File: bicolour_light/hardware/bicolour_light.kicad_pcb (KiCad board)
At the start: 2 copper layers, 12.6 x 11 mm, 6 parts, among them J1 PIN_A, J2 PIN_B

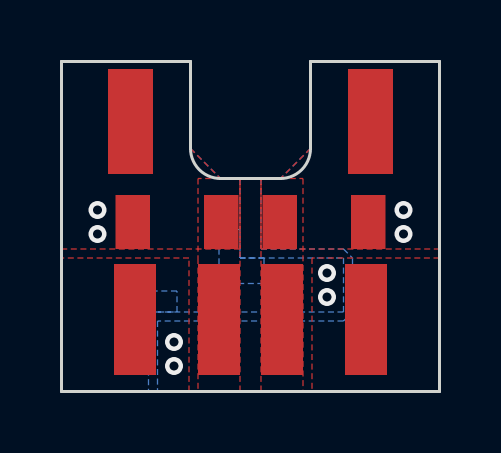
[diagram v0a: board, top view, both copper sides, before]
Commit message: Added polar light (single yellow LED)
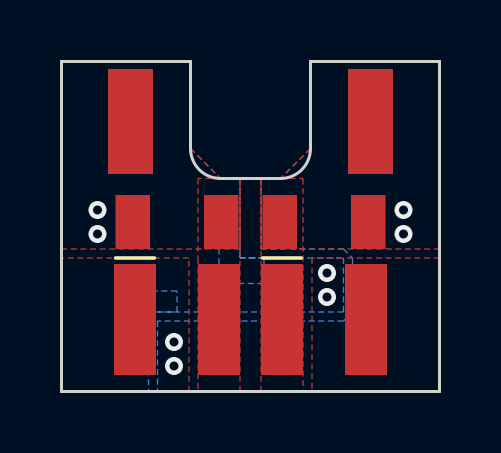
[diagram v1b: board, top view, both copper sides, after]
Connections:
- D1 pad 1: Net-(D1-KA) -> /PIN_B
- D1 pad 2: /PIN_B -> Net-(D1-AK)
- D2 pad 1: /PIN_A -> Net-(D2-KA)
- D2 pad 2: Net-(D2-AK) -> /PIN_A
- R1 pad 2: Net-(D1-KA) -> Net-(D1-AK)
- R2 pad 1: Net-(D2-AK) -> Net-(D2-KA)
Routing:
- added copper zone on F.Cu, net Net-(D1-AK)
- added copper zone on F.Cu, net Net-(D2-KA)
- removed copper zone on F.Cu, net Net-(D1-KA)
- removed copper zone on F.Cu, net Net-(D2-AK)
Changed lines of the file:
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@@
   (net 1 "/PIN_B")
   (net 2 "/PIN_A")
-  (net 3 "Net-(D1-KA)")
-  (net 4 "Net-(D2-AK)")
+  (net 3 "Net-(D1-AK)")
+  (net 4 "Net-(D2-KA)")
   (footprint "Slonket_Footprints:D_LED_4040" (layer "F.Cu")
     (at 126.65 94.55 180)
     (property "LCSC" "C7545694")
-    (property "Sheetfile" "LED_light.kicad_sch")
+    (property "Sheetfile" "bicolour_light.kicad_sch")
     (property "Sheetname" "")
     (property "ki_description" "Dual LED, bidirectional")
@@
         (effects (font (size 0.75 0.75) (thickness 0.1)))
     )
+    (fp_line (start 2.05 2.4) (end 0.75 2.4)
+      (stroke (width 0.12) (type default)) (layer "F.SilkS"))
     (fp_rect (start -2.35 2.45) (end 2.35 -2.05)
       (stroke (width 0.05) (type default)) (fill none) (layer "F.CrtYd"))
-    (fp_line (start -2 -1.3) (end -1.5 -1.8)
-      (stroke (width 0.1) (type default)) (layer "F.Fab"))
-    (fp_line (start -2 1.8) (end -2 -1.3)
-      (stroke (width 0.1) (type default)) (layer "F.Fab"))
-    (fp_line (start -1.5 -1.8) (end 2 -1.8)
-      (stroke (width 0.1) (type default)) (layer "F.Fab"))
-    (fp_line (start 2 -1.8) (end 2 1.8)
-      (stroke (width 0.1) (type default)) (layer "F.Fab"))
-    (fp_line (start 2 1.8) (end -2 1.8)
-      (stroke (width 0.1) (type default)) (layer "F.Fab"))
-    (pad "1" smd rect (at -1.4 0.35 180) (size 1.4 3.7) (layers "F.Cu" "F.Paste" "F.Mask")
-      (net 3 "Net-(D1-KA)") (pinfunction "KA") (pintype "input") (thermal_bridge_angle 45))
-    (pad "2" smd rect (at 1.4 0.35 180) (size 1.4 3.7) (layers "F.Cu" "F.Paste" "F.Mask")
-      (net 1 "/PIN_B") (pinfunction "AK") (pintype "input") (thermal_bridge_angle 45))
+    (fp_line (start -2 -1.8) (end 2 -1.8)
+      (stroke (width 0.1) (type default)) (layer "F.Fab"))
+    (fp_line (start -2 1.8) (end -2 -1.8)
+      (stroke (width 0.1) (type default)) (layer "F.Fab"))
+    (fp_line (start 1.5 1.8) (end -2 1.8)
+      (stroke (width 0.1) (type default)) (layer "F.Fab"))
+    (fp_line (start 2 -1.8) (end 2 1.3)
+      (stroke (width 0.1) (type default)) (layer "F.Fab"))
+    (fp_line (start 2 1.3) (end 1.5 1.8)
+      (stroke (width 0.1) (type default)) (layer "F.Fab"))
+    (pad "1" smd rect (at 1.4 0.35 180) (size 1.4 3.7) (layers "F.Cu" "F.Paste" "F.Mask")
+      (net 1 "/PIN_B") (pinfunction "KA") (pintype "input") (thermal_bridge_angle 45))
+    (pad "2" smd rect (at -1.4 0.35 180) (size 1.4 3.7) (layers "F.Cu" "F.Paste" "F.Mask")
+      (net 3 "Net-(D1-AK)") (pinfunction "AK") (pintype "input") (thermal_bridge_angle 45))
     (model "../3D_models/LED4040.step"
       (offset (xyz 0 1.8 0))
@@
     (at 126.65 90.95)
     (property "LCSC" "C25386")
-    (property "Sheetfile" "LED_light.kicad_sch")
+    (property "Sheetfile" "bicolour_light.kicad_sch")
     (property "Sheetname" "")
     (property "ki_description" "Resistor")
@@
       (net 2 "/PIN_A") (pintype "passive"))
     (pad "2" smd rect (at 1.475 0) (size 1.15 1.8) (layers "F.Cu" "F.Paste" "F.Mask")
-      (net 3 "Net-(D1-KA)") (pintype "passive"))
+      (net 3 "Net-(D1-AK)") (pintype "passive"))
     (model "${KICAD6_3DMODEL_DIR}/Resistor_SMD.3dshapes/R_1206_3216Metric.wrl"
       (offset (xyz 0 0 0))
@@
     (at 131.55 90.95)
     (property "LCSC" "C25386")
-    (property "Sheetfile" "LED_light.kicad_sch")
+    (property "Sheetfile" "bicolour_light.kicad_sch")
     (property "Sheetname" "")
     (property "ki_description" "Resistor")
@@
       (stroke (width 0.1) (type solid)) (layer "F.Fab"))
     (pad "1" smd rect (at -1.475 0) (size 1.15 1.8) (layers "F.Cu" "F.Paste" "F.Mask")
-      (net 4 "Net-(D2-AK)") (pintype "passive"))
+      (net 4 "Net-(D2-KA)") (pintype "passive"))
     (pad "2" smd rect (at 1.475 0) (size 1.15 1.8) (layers "F.Cu" "F.Paste" "F.Mask")
       (net 1 "/PIN_B") (pintype "passive"))
@@
   (footprint "Slonket_Footprints:J_Pad_1_Lego" (layer "F.Cu")
     (at 125.1 87.6 180)
-    (property "Sheetfile" "LED_light.kicad_sch")
+    (property "Sheetfile" "bicolour_light.kicad_sch")
     (property "Sheetname" "")
     (property "ki_description" "Generic connector, single row, 01x01, script generated (kicad-library-utils/schlib/autogen/connector/)")
@@
     (at 131.55 94.55 180)
     (property "LCSC" "C7545694")
-    (property "Sheetfile" "LED_light.kicad_sch")
+    (property "Sheetfile" "bicolour_light.kicad_sch")
     (property "Sheetname" "")
     (property "ki_description" "Dual LED, bidirectional")
@@
         (effects (font (size 0.75 0.75) (thickness 0.1)))
     )
+    (fp_line (start 2.05 2.4) (end 0.75 2.4)
+      (stroke (width 0.12) (type default)) (layer "F.SilkS"))
     (fp_rect (start -2.35 2.45) (end 2.35 -2.05)
       (stroke (width 0.05) (type default)) (fill none) (layer "F.CrtYd"))
-    (fp_line (start -2 -1.3) (end -1.5 -1.8)
-      (stroke (width 0.1) (type default)) (layer "F.Fab"))
-    (fp_line (start -2 1.8) (end -2 -1.3)
-      (stroke (width 0.1) (type default)) (layer "F.Fab"))
-    (fp_line (start -1.5 -1.8) (end 2 -1.8)
-      (stroke (width 0.1) (type default)) (layer "F.Fab"))
-    (fp_line (start 2 -1.8) (end 2 1.8)
-      (stroke (width 0.1) (type default)) (layer "F.Fab"))
-    (fp_line (start 2 1.8) (end -2 1.8)
-      (stroke (width 0.1) (type default)) (layer "F.Fab"))
-    (pad "1" smd rect (at -1.4 0.35 180) (size 1.4 3.7) (layers "F.Cu" "F.Paste" "F.Mask")
-      (net 2 "/PIN_A") (pinfunction "KA") (pintype "input") (thermal_bridge_angle 45))
-    (pad "2" smd rect (at 1.4 0.35 180) (size 1.4 3.7) (layers "F.Cu" "F.Paste" "F.Mask")
-      (net 4 "Net-(D2-AK)") (pinfunction "AK") (pintype "input") (thermal_bridge_angle 45))
+    (fp_line (start -2 -1.8) (end 2 -1.8)
+      (stroke (width 0.1) (type default)) (layer "F.Fab"))
+    (fp_line (start -2 1.8) (end -2 -1.8)
+      (stroke (width 0.1) (type default)) (layer "F.Fab"))
+    (fp_line (start 1.5 1.8) (end -2 1.8)
+      (stroke (width 0.1) (type default)) (layer "F.Fab"))
+    (fp_line (start 2 -1.8) (end 2 1.3)
+      (stroke (width 0.1) (type default)) (layer "F.Fab"))
+    (fp_line (start 2 1.3) (end 1.5 1.8)
+      (stroke (width 0.1) (type default)) (layer "F.Fab"))
+    (pad "1" smd rect (at 1.4 0.35 180) (size 1.4 3.7) (layers "F.Cu" "F.Paste" "F.Mask")
+      (net 4 "Net-(D2-KA)") (pinfunction "KA") (pintype "input") (thermal_bridge_angle 45))
+    (pad "2" smd rect (at -1.4 0.35 180) (size 1.4 3.7) (layers "F.Cu" "F.Paste" "F.Mask")
+      (net 2 "/PIN_A") (pinfunction "AK") (pintype "input") (thermal_bridge_angle 45))
     (model "../3D_models/LED4040.step"
       (offset (xyz 0 1.8 0))
@@
   (footprint "Slonket_Footprints:J_Pad_1_Lego" (layer "F.Cu")
     (at 133.1 87.6 180)
-    (property "Sheetfile" "LED_light.kicad_sch")
+    (property "Sheetfile" "bicolour_light.kicad_sch")
     (property "Sheetname" "")
     (property "ki_description" "Generic connector, single row, 01x01, script generated (kicad-library-utils/schlib/autogen/connector/)")
@@
   (via (at 124 90.55) (size 0.6) (drill 0.3) (layers "F.Cu" "B.Cu") (free) (net 2))
   (via (at 124 91.35) (size 0.6) (drill 0.3) (layers "F.Cu" "B.Cu") (free) (net 2))
-  (zone (net 3) (net_name "Net-(D1-KA)") (layer "F.Cu") (hatch edge 0.5)
+  (zone (net 3) (net_name "Net-(D1-AK)") (layer "F.Cu") (hatch edge 0.5)
     (priority 2)
     (connect_pads yes (clearance 0.2))
@@
     )
   )
-  (zone (net 4) (net_name "Net-(D2-AK)") (layer "F.Cu") (hatch edge 0.5)
+  (zone (net 4) (net_name "Net-(D2-KA)") (layer "F.Cu") (hatch edge 0.5)
     (priority 2)
     (connect_pads yes (clearance 0.2))
